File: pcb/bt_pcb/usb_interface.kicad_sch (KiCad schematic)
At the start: 8 parts, among them J6 UJ32-C-H-G-SMT-TR-68

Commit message: first notes
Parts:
- removed J6: UJ32-C-H-G-SMT-TR-68, library:UJ32CHGSMTTR68, symbol library:UJ32-C-H-G-SMT-TR-68
- added J6: USB_C_Receptacle_USB2.0_16P, Connector_USB:USB_C_Receptacle_GCT_USB4105-xx-A_16P_TopMnt_Horizontal, symbol Connector:USB_C_Receptacle_USB2.0_16P
- renumbered R9 to R10, R10 to R9
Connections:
- net GND: now also J6.A1 (GND), J6.A12 (GND), J6.A8 (SBU1), J6.B1 (GND), J6.B12 (GND), J6.B8 (SBU2), J6.S1 (SHIELD)
- net USB_D+: now also J6.A7 (D-), J6.B7 (D-)
- net USB_D-: now also J6.A6 (D+), J6.B6 (D+)
- net VBUS: now also J6.A4 (VBUS), J6.A9 (VBUS), J6.B4 (VBUS), J6.B9 (VBUS)
- net at R9.1: now also J6.B5 (CC2)
- net at R10.1: now also J6.A5 (CC1)
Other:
- moved on the sheet: R10, R9

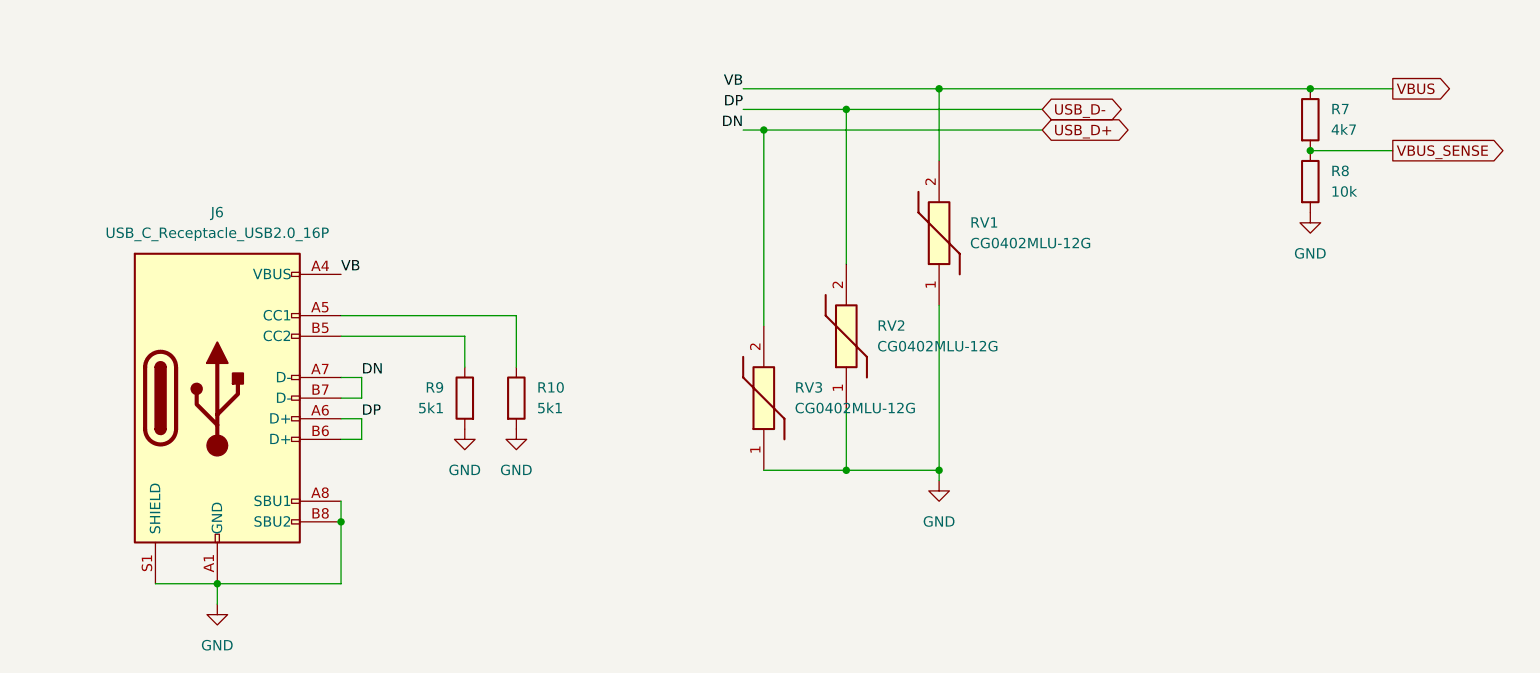
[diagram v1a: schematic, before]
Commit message: doing pcb from scratch again
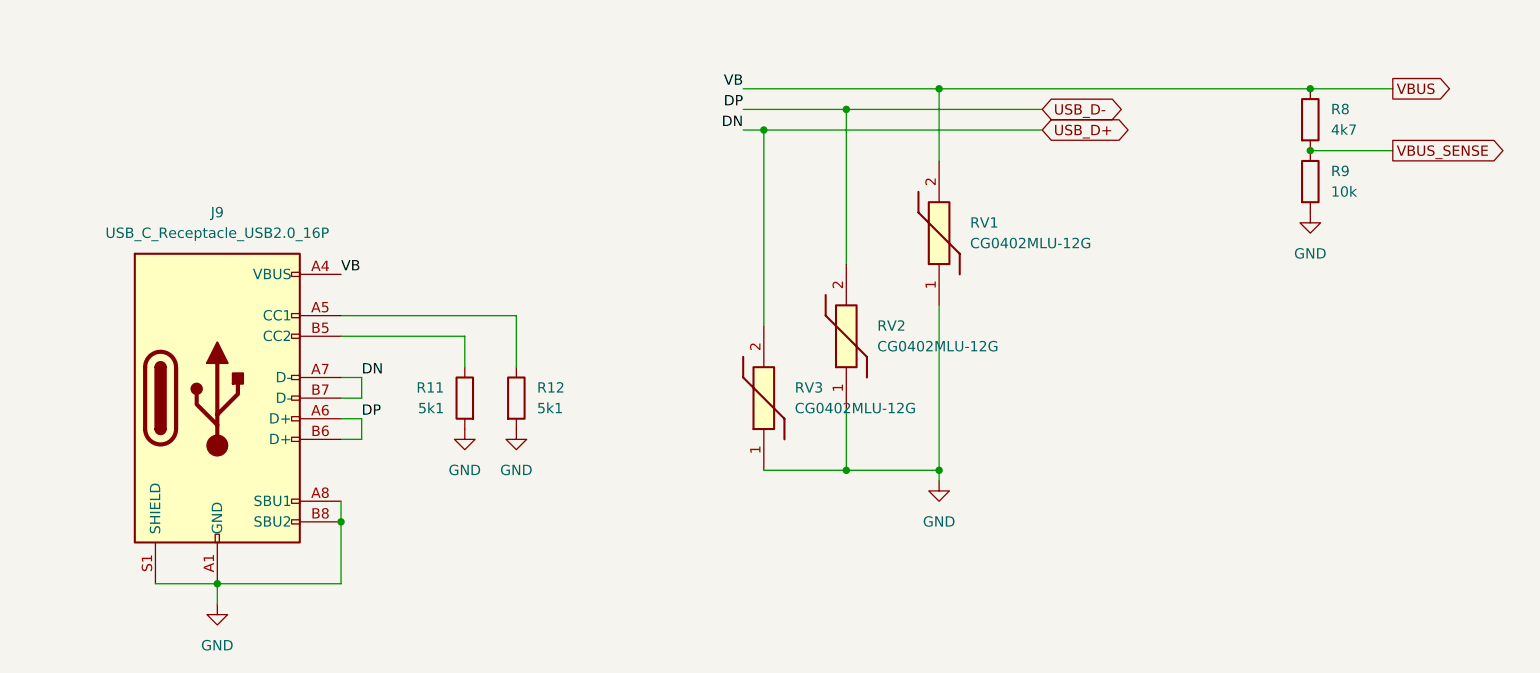
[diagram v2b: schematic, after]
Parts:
- renumbered J6 to J9, R9 to R11, R10 to R12, R7 to R8, R8 to R9
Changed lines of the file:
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@@
 		(on_board yes)
 		(dnp no)
-		(property "Reference" "R9"
+		(property "Reference" "R11"
 			(at 124.46 86.36 0)
 			(effects
@@
 			(project "bt_pcb"
 				(path "/eb787481-08cd-41a4-a128-173fa6227c32/81f44120-5006-4955-ab2c-f15dbf34b899"
-					(reference "R9")
+					(reference "R11")
 					(unit 1)
 				)
@@
 		(dnp no)
 		(fields_autoplaced yes)
-		(property "Reference" "#PWR034"
+		(property "Reference" "#PWR043"
 			(at 185.42 104.14 0)
 			(effects
@@
 			(project "bt_pcb"
 				(path "/eb787481-08cd-41a4-a128-173fa6227c32/81f44120-5006-4955-ab2c-f15dbf34b899"
-					(reference "#PWR034")
+					(reference "#PWR043")
 					(unit 1)
 				)
@@
 		(dnp no)
 		(fields_autoplaced yes)
-		(property "Reference" "J6"
+		(property "Reference" "J9"
 			(at 96.52 64.77 0)
 			(effects
@@
 			(project ""
 				(path "/eb787481-08cd-41a4-a128-173fa6227c32/81f44120-5006-4955-ab2c-f15dbf34b899"
-					(reference "J6")
+					(reference "J9")
 					(unit 1)
 				)
@@
 		(dnp no)
 		(fields_autoplaced yes)
-		(property "Reference" "#PWR031"
+		(property "Reference" "#PWR037"
 			(at 231.14 71.12 0)
 			(effects
@@
 			(project "bt_pcb"
 				(path "/eb787481-08cd-41a4-a128-173fa6227c32/81f44120-5006-4955-ab2c-f15dbf34b899"
-					(reference "#PWR031")
+					(reference "#PWR037")
 					(unit 1)
 				)
@@
 		(dnp no)
 		(fields_autoplaced yes)
-		(property "Reference" "#PWR033"
+		(property "Reference" "#PWR042"
 			(at 133.35 97.79 0)
 			(effects
@@
 			(project "bt_pcb"
 				(path "/eb787481-08cd-41a4-a128-173fa6227c32/81f44120-5006-4955-ab2c-f15dbf34b899"
-					(reference "#PWR033")
+					(reference "#PWR042")
 					(unit 1)
 				)
@@
 		(dnp no)
 		(fields_autoplaced yes)
-		(property "Reference" "R7"
+		(property "Reference" "R8"
 			(at 233.68 52.07 0)
 			(effects
@@
 			(project "bt_pcb"
 				(path "/eb787481-08cd-41a4-a128-173fa6227c32/81f44120-5006-4955-ab2c-f15dbf34b899"
-					(reference "R7")
+					(reference "R8")
 					(unit 1)
 				)
@@
 		(dnp no)
 		(fields_autoplaced yes)
-		(property "Reference" "#PWR035"
+		(property "Reference" "#PWR046"
 			(at 96.52 119.38 0)
 			(effects
@@
 			(project "bt_pcb"
 				(path "/eb787481-08cd-41a4-a128-173fa6227c32/81f44120-5006-4955-ab2c-f15dbf34b899"
-					(reference "#PWR035")
+					(reference "#PWR046")
 					(unit 1)
 				)
@@
 		(dnp no)
 		(fields_autoplaced yes)
-		(property "Reference" "R8"
+		(property "Reference" "R9"
 			(at 233.68 59.69 0)
 			(effects
@@
 			(project "bt_pcb"
 				(path "/eb787481-08cd-41a4-a128-173fa6227c32/81f44120-5006-4955-ab2c-f15dbf34b899"
-					(reference "R8")
+					(reference "R9")
 					(unit 1)
 				)
@@
 		(dnp no)
 		(fields_autoplaced yes)
-		(property "Reference" "#PWR032"
+		(property "Reference" "#PWR041"
 			(at 127 97.79 0)
 			(effects
@@
 			(project "bt_pcb"
 				(path "/eb787481-08cd-41a4-a128-173fa6227c32/81f44120-5006-4955-ab2c-f15dbf34b899"
-					(reference "#PWR032")
+					(reference "#PWR041")
 					(unit 1)
 				)
@@
 		(dnp no)
 		(fields_autoplaced yes)
-		(property "Reference" "R10"
+		(property "Reference" "R12"
 			(at 135.89 86.36 0)
 			(effects
@@
 			(project "bt_pcb"
 				(path "/eb787481-08cd-41a4-a128-173fa6227c32/81f44120-5006-4955-ab2c-f15dbf34b899"
-					(reference "R10")
-					(unit 1)
-				)
+					(reference "R12")
+					(unit 1)
+				)

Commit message: redo of power supply
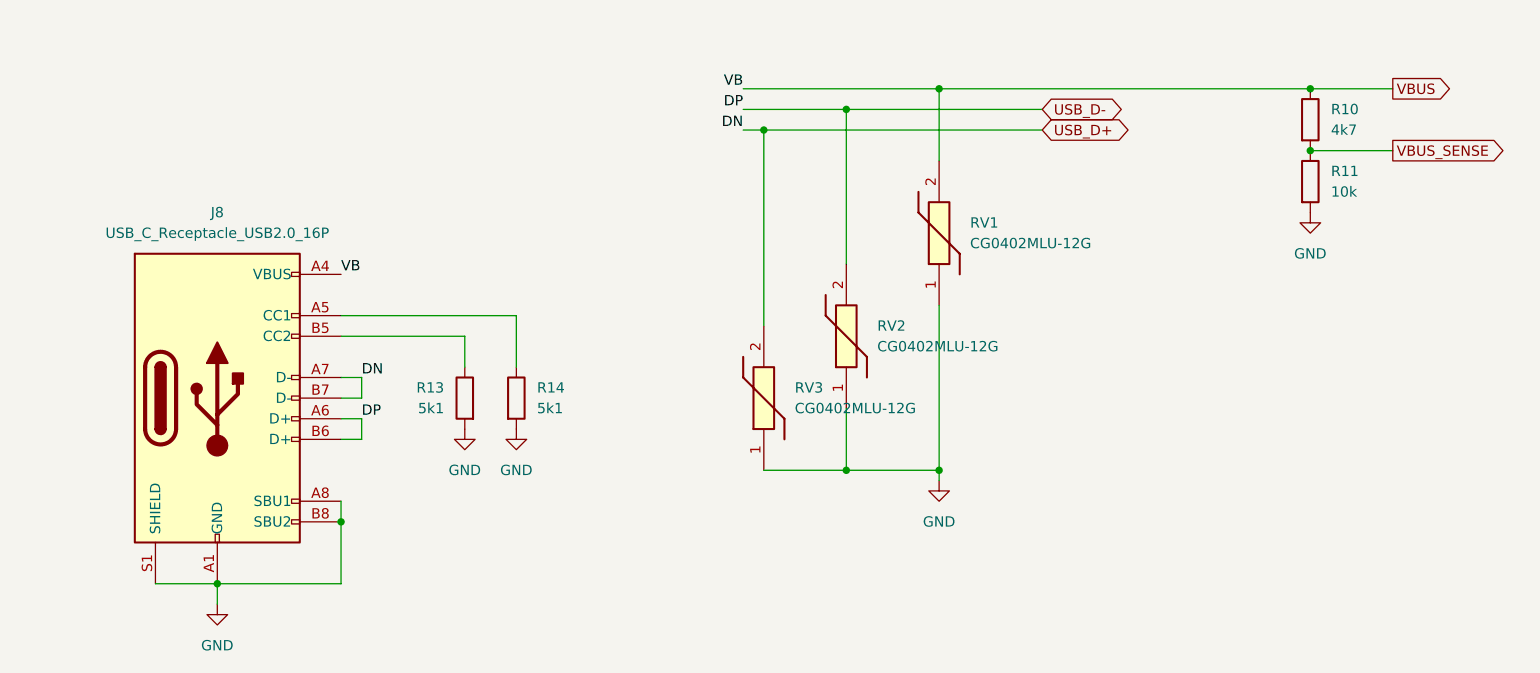
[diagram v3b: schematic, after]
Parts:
- renumbered J9 to J8, R8 to R10, R9 to R11, R11 to R13, R12 to R14
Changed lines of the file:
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@@
 		(on_board yes)
 		(dnp no)
-		(property "Reference" "R11"
+		(property "Reference" "R13"
 			(at 124.46 86.36 0)
 			(effects
@@
 			(project "bt_pcb"
 				(path "/eb787481-08cd-41a4-a128-173fa6227c32/81f44120-5006-4955-ab2c-f15dbf34b899"
-					(reference "R11")
+					(reference "R13")
 					(unit 1)
 				)
@@
 		(dnp no)
 		(fields_autoplaced yes)
-		(property "Reference" "#PWR043"
+		(property "Reference" "#PWR045"
 			(at 185.42 104.14 0)
 			(effects
@@
 			(project "bt_pcb"
 				(path "/eb787481-08cd-41a4-a128-173fa6227c32/81f44120-5006-4955-ab2c-f15dbf34b899"
-					(reference "#PWR043")
+					(reference "#PWR045")
 					(unit 1)
 				)
@@
 		(dnp no)
 		(fields_autoplaced yes)
-		(property "Reference" "J9"
+		(property "Reference" "J8"
 			(at 96.52 64.77 0)
 			(effects
@@
 			(project ""
 				(path "/eb787481-08cd-41a4-a128-173fa6227c32/81f44120-5006-4955-ab2c-f15dbf34b899"
-					(reference "J9")
+					(reference "J8")
 					(unit 1)
 				)
@@
 		(dnp no)
 		(fields_autoplaced yes)
-		(property "Reference" "#PWR037"
+		(property "Reference" "#PWR039"
 			(at 231.14 71.12 0)
 			(effects
@@
 			(project "bt_pcb"
 				(path "/eb787481-08cd-41a4-a128-173fa6227c32/81f44120-5006-4955-ab2c-f15dbf34b899"
-					(reference "#PWR037")
+					(reference "#PWR039")
 					(unit 1)
 				)
@@
 		(dnp no)
 		(fields_autoplaced yes)
-		(property "Reference" "#PWR042"
+		(property "Reference" "#PWR044"
 			(at 133.35 97.79 0)
 			(effects
@@
 			(project "bt_pcb"
 				(path "/eb787481-08cd-41a4-a128-173fa6227c32/81f44120-5006-4955-ab2c-f15dbf34b899"
-					(reference "#PWR042")
+					(reference "#PWR044")
 					(unit 1)
 				)
@@
 		(dnp no)
 		(fields_autoplaced yes)
-		(property "Reference" "R8"
+		(property "Reference" "R10"
 			(at 233.68 52.07 0)
 			(effects
@@
 			(project "bt_pcb"
 				(path "/eb787481-08cd-41a4-a128-173fa6227c32/81f44120-5006-4955-ab2c-f15dbf34b899"
-					(reference "R8")
+					(reference "R10")
 					(unit 1)
 				)
@@
 		(dnp no)
 		(fields_autoplaced yes)
-		(property "Reference" "#PWR046"
+		(property "Reference" "#PWR048"
 			(at 96.52 119.38 0)
 			(effects
@@
 			(project "bt_pcb"
 				(path "/eb787481-08cd-41a4-a128-173fa6227c32/81f44120-5006-4955-ab2c-f15dbf34b899"
-					(reference "#PWR046")
+					(reference "#PWR048")
 					(unit 1)
 				)
@@
 		(dnp no)
 		(fields_autoplaced yes)
-		(property "Reference" "R9"
+		(property "Reference" "R11"
 			(at 233.68 59.69 0)
 			(effects
@@
 			(project "bt_pcb"
 				(path "/eb787481-08cd-41a4-a128-173fa6227c32/81f44120-5006-4955-ab2c-f15dbf34b899"
-					(reference "R9")
+					(reference "R11")
 					(unit 1)
 				)
@@
 		(dnp no)
 		(fields_autoplaced yes)
-		(property "Reference" "#PWR041"
+		(property "Reference" "#PWR043"
 			(at 127 97.79 0)
 			(effects
@@
 			(project "bt_pcb"
 				(path "/eb787481-08cd-41a4-a128-173fa6227c32/81f44120-5006-4955-ab2c-f15dbf34b899"
-					(reference "#PWR041")
+					(reference "#PWR043")
 					(unit 1)
 				)
@@
 		(dnp no)
 		(fields_autoplaced yes)
-		(property "Reference" "R12"
+		(property "Reference" "R14"
 			(at 135.89 86.36 0)
 			(effects
@@
 			(project "bt_pcb"
 				(path "/eb787481-08cd-41a4-a128-173fa6227c32/81f44120-5006-4955-ab2c-f15dbf34b899"
-					(reference "R12")
-					(unit 1)
-				)
+					(reference "R14")
+					(unit 1)
+				)

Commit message: aaaaaaa
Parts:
- renumbered J8 to J7, R13 to R16, R14 to R17, R10 to R26, R11 to R27, RV3 to RV1, RV1 to RV3

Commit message: schematic rev b finish?
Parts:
- removed R16: 5k1, Resistor_SMD:R_0603_1608Metric_Pad0.98x0.95mm_HandSolder, symbol Device:R
- added R10: 5k1, Resistor_SMD:R_0603_1608Metric_Pad0.98x0.95mm_HandSolder, symbol Device:R
- renumbered R27 to R11, R26 to R8, R17 to R9, RV3 to RV1, RV1 to RV3
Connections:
- net GND: now also J7.SH (SHIELD), R10.2; no longer J7.S1 (SHIELD)
- net USB_D+: now also J7.A6 (D+), J7.B6 (D+); no longer J7.A7 (D-), J7.B7 (D-)
- net USB_D-: now also J7.A7 (D-), J7.B7 (D-); no longer J7.A6 (D+), J7.B6 (D+)
- net at J7.B5 (CC2): now also R10.1
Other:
- moved on the sheet: J7, R9, RV1, RV2, RV3

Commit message: progress!
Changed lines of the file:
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@@
 	(wire
 		(pts
-			(xy 95.25 87.63) (xy 95.25 90.17)
+			(xy 95.25 87.63) (xy 95.25 91.44)
 		)
 		(stroke
@@
 		(lib_name "GND_1")
 		(lib_id "power:GND")
-		(at 95.25 90.17 0)
+		(at 95.25 91.44 0)
 		(unit 1)
 		(body_style 1)
@@
 		(fields_autoplaced yes)
 		(property "Reference" "#PWR067"
+			(at 95.25 97.79 0)
+			(hide yes)
+			(show_name no)
+			(do_not_autoplace no)
+			(effects
+				(font
+					(size 1.27 1.27)
+				)
+			)
+		)
+		(property "Value" "GND"
 			(at 95.25 96.52 0)
-			(hide yes)
-			(show_name no)
-			(do_not_autoplace no)
-			(effects
-				(font
-					(size 1.27 1.27)
-				)
-			)
-		)
-		(property "Value" "GND"
-			(at 95.25 95.25 0)
 			(show_name no)
 			(do_not_autoplace no)
@@
 		)
 		(property "Footprint" ""
-			(at 95.25 90.17 0)
+			(at 95.25 91.44 0)
 			(hide yes)
 			(show_name no)
@@
 		)
 		(property "Datasheet" ""
-			(at 95.25 90.17 0)
+			(at 95.25 91.44 0)
 			(hide yes)
 			(show_name no)
@@
 		)
 		(property "Description" "Power symbol creates a global label with name \"GND\" , ground"
-			(at 95.25 90.17 0)
-			(hide yes)
-			(show_name no)
+			(at 95.25 91.44 0)
+			(hide yes)
+			(show_name no)

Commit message: sd kind of in
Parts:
- renumbered R8 to R5, R9 to R6, R10 to R7, R11 to R8
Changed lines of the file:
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@@
 		(dnp no)
 		(fields_autoplaced yes)
-		(property "Reference" "R8"
+		(property "Reference" "R5"
 			(at 233.68 52.07 0)
 			(show_name no)
@@
 			(project "bt_pcb"
 				(path "/eb787481-08cd-41a4-a128-173fa6227c32/81f44120-5006-4955-ab2c-f15dbf34b899"
-					(reference "R8")
+					(reference "R5")
 					(unit 1)
 				)
@@
 		(in_pos_files yes)
 		(dnp no)
-		(property "Reference" "R10"
+		(property "Reference" "R7"
 			(at 133.35 50.8 90)
 			(show_name no)
@@
 			(project "bt_pcb"
 				(path "/eb787481-08cd-41a4-a128-173fa6227c32/81f44120-5006-4955-ab2c-f15dbf34b899"
-					(reference "R10")
+					(reference "R7")
 					(unit 1)
 				)
@@
 		(dnp no)
 		(fields_autoplaced yes)
-		(property "Reference" "R11"
+		(property "Reference" "R8"
 			(at 233.68 59.69 0)
 			(show_name no)
@@
 			(project "bt_pcb"
 				(path "/eb787481-08cd-41a4-a128-173fa6227c32/81f44120-5006-4955-ab2c-f15dbf34b899"
-					(reference "R11")
+					(reference "R8")
 					(unit 1)
 				)
@@
 		(dnp no)
 		(fields_autoplaced yes)
-		(property "Reference" "R9"
+		(property "Reference" "R6"
 			(at 142.24 48.26 90)
 			(show_name no)
@@
 			(project "bt_pcb"
 				(path "/eb787481-08cd-41a4-a128-173fa6227c32/81f44120-5006-4955-ab2c-f15dbf34b899"
-					(reference "R9")
+					(reference "R6")
 					(unit 1)
 				)
